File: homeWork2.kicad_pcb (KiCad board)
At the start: 2 copper layers, 130 x 100 mm, 49 parts, among them J1 Barrel_Jack_Switch_SMT, J2 0.100_2Pin, J3 0.100_2Pin, U1 LM7805_TO220

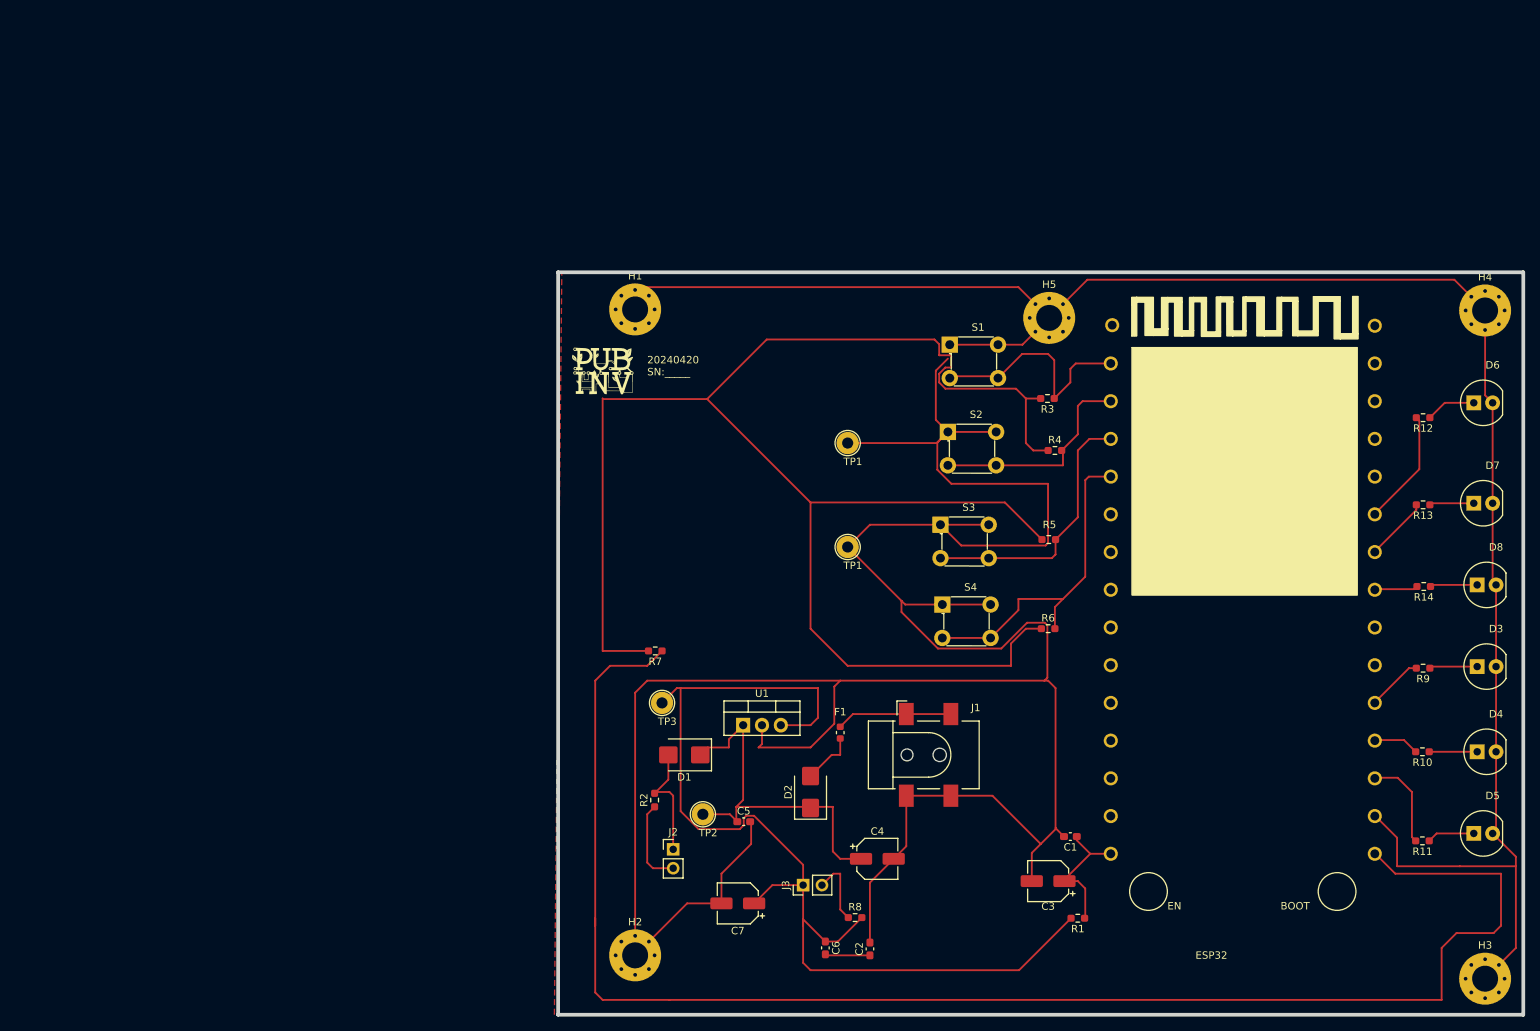
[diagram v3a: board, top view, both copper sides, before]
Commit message: I removed the ground traces and applied copper fill on both the front and back copper layers to establish the ground connections. Additionally, I updated the footprint of the ESP32, positioning the antenna within an area free from copper ground connections, and added four holes along its edges.
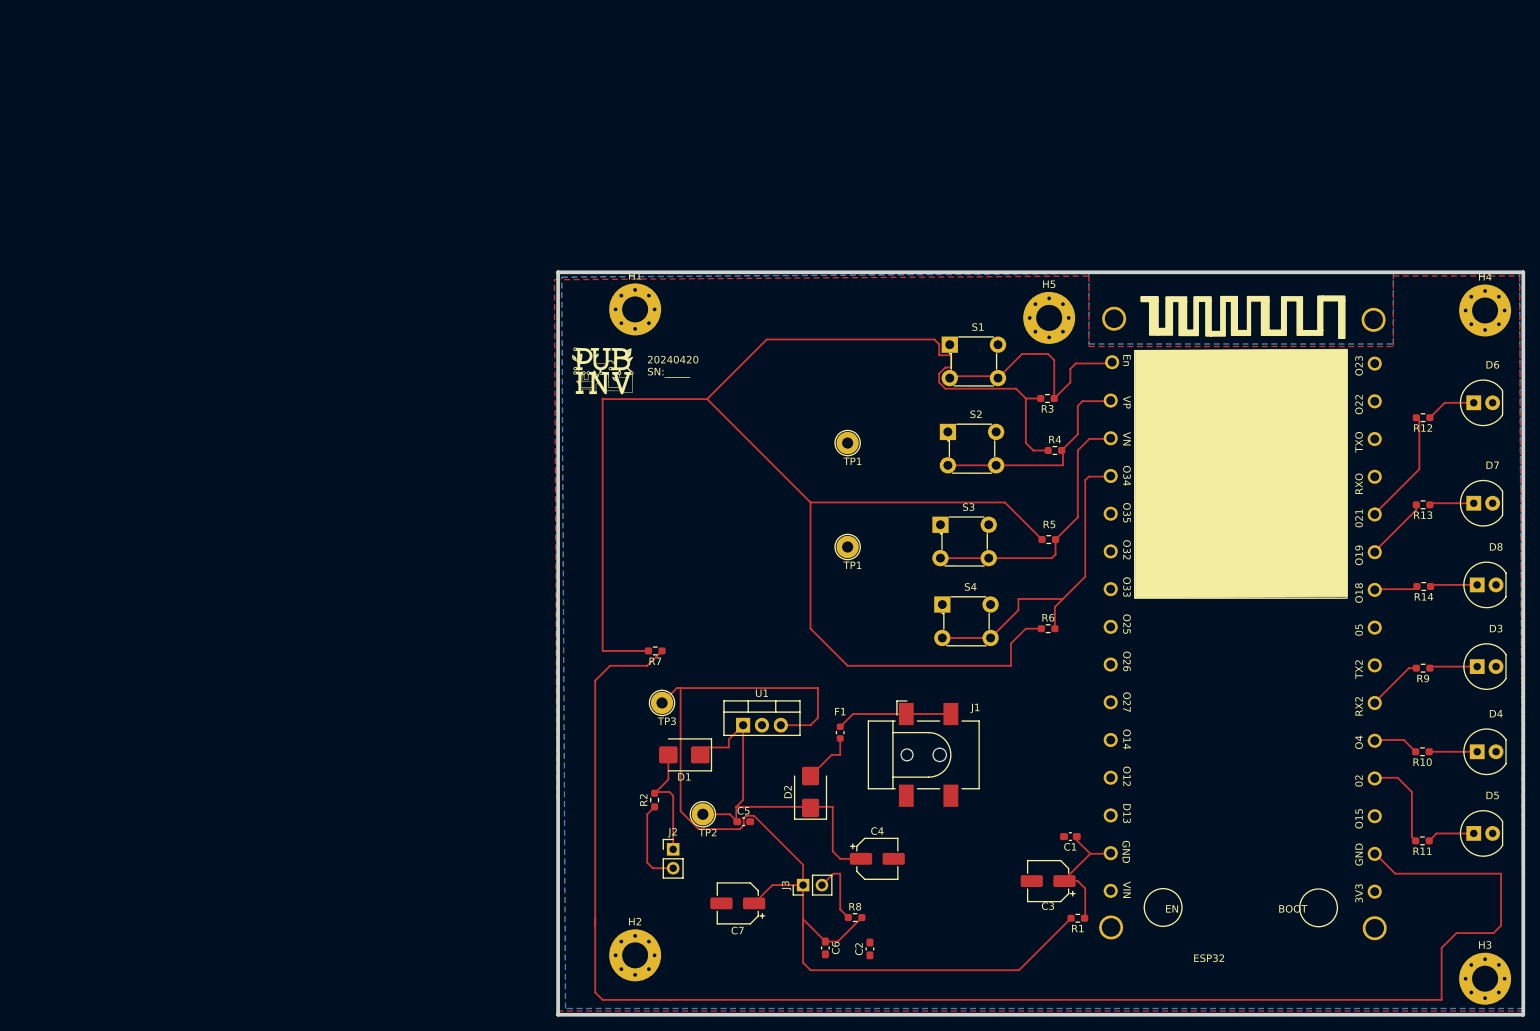
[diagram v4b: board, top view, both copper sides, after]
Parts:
- moved ESP32 0.53 mm to (211.9, 47.5)
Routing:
- net GND: track 625.6 -> 0.19 mm
- added copper zone on B.Cu, net GND

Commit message: I updated the ESP32 footprint and symbol, renamed the pins of the ESP32 in a clockwise direction. I rerouted the copper, and ran a DRC test with zero errors and refined the edge cut of the board to make it smaller and neater.
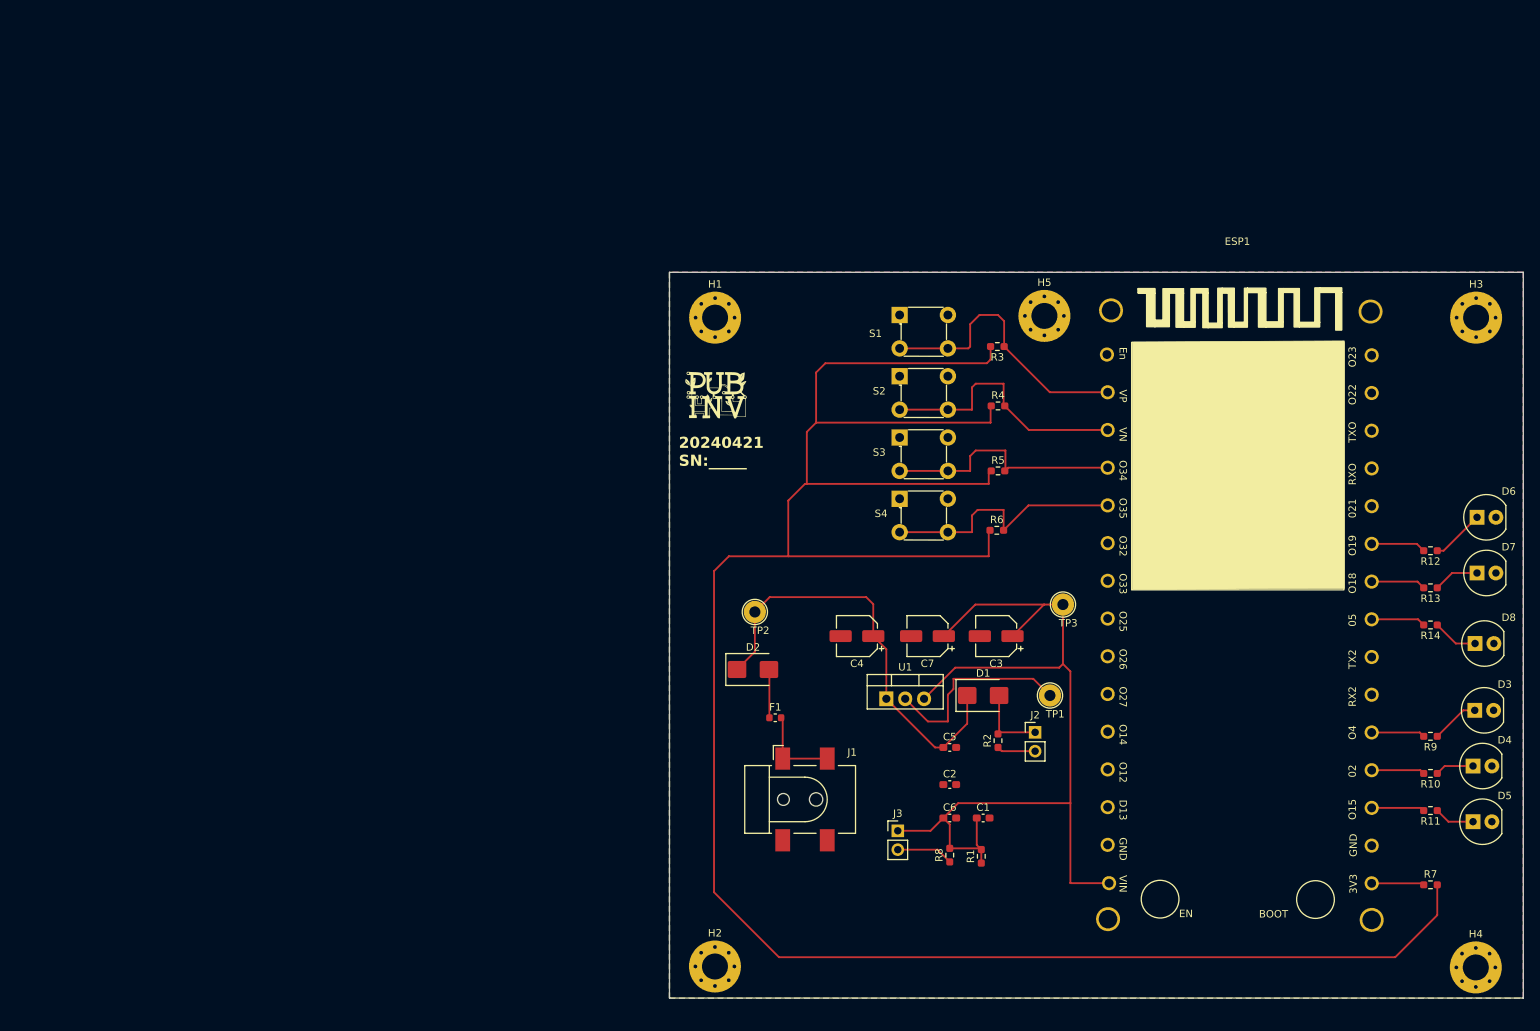
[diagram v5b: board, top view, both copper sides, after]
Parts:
- removed ESP32: Wroom ESP32, esp32 15 pin Library:esp32
- removed the TP1 at (159.0, 73.0)
- removed the TP1 at (159.0, 87.0)
- added ESP1: ~, esp32 15 pin Library:esp32, F.Cu at (211.5, 46.3)
- added TP1: TestPoint, TestPoint:TestPoint_Loop_D2.54mm_Drill1.5mm_Beaded, F.Cu at (186.2, 107.0)
- C1, C5, C6: value 100nF -> C
- C2: value 39pF -> C
- C3, C4, C7: value 47uF 16V -> C_Polarized
- D1, D2: value Schottky 2A -> D_Schottky
- R1, R7: value 1R0 -> R
- R10, R11, R12, R13, R14, R9: value 330R -> R
- R2, R8: value DNI -> R
- R3, R4, R5, R6: value 10K -> R
- TP2: value Vin -> TestPoint
- TP3: value +5V -> TestPoint
- moved R7 109.1 mm to (237.5, 132.5), turned to 0 degrees
- moved H3 89.0 mm to (243.6, 56.1)
- moved H4 88.5 mm to (243.6, 143.6)
- moved TP3 55.6 mm to (188.0, 94.8)
- moved J2 51.2 mm to (184.2, 112.0)
- moved R2 46.9 mm to (179.2, 113.1)
- moved C7 44.1 mm to (169.8, 99.0)
- moved D1 41.0 mm to (177.2, 107.0), turned to 0 degrees
- moved C3 33.7 mm to (179.0, 99.0)
- moved C4 30.1 mm to (160.2, 99.0), turned to 180 degrees
- moved C5 29.5 mm to (172.8, 114.0)
- moved TP2 28.1 mm to (146.5, 95.8)
- moved C2 24.6 mm to (172.8, 119.0), turned to 0 degrees
- moved C6 24.2 mm to (172.8, 123.5), turned to 0 degrees
- moved U1 19.6 mm to (164.2, 107.4)
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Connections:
- C1 pad 1: Net-(ESP1-VIN) -> +5V
- C3 pad 1: Net-(ESP1-VIN) -> +5V
- R1 pad 1: Net-(ESP1-VIN) -> +5V
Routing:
- net Net-(ESP1-3V3): track 209.6 -> 7.09 mm
- net +3.3V: track 227.9 -> 296.7 mm
- net GND: track 0.19 -> 27.0 mm
- net Net-(ESP1-VIN): track 18.2 -> 0.00 mm
- net +5V: track 140.9 -> 127.5 mm
- net Net-(ESP1-O35): track 44.6 -> 34.7 mm
- net Vin: track 49.9 -> 58.1 mm
- net Net-(ESP1-O19): track 15.6 -> 7.39 mm
- net ControllerVcc: track 11.7 -> 5.21 mm
- net Net-(ESP1-VP): track 31.6 -> 38.0 mm
- net Net-(ESP1-VN): track 29.2 -> 35.5 mm
- net Net-(D1-A): track 15.9 -> 10.3 mm
- net Net-(ESP1-O15): track 12.6 -> 7.16 mm
- net Net-(F1-Pad2): track 15.6 -> 11.6 mm
- net Net-(ESP1-O34): track 36.0 -> 33.4 mm
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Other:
- board size 130 x 100 mm -> 115 x 97.8 mm
- board text added: "20240421 SN:_____"
- board text removed: "20240420 SN:_____"

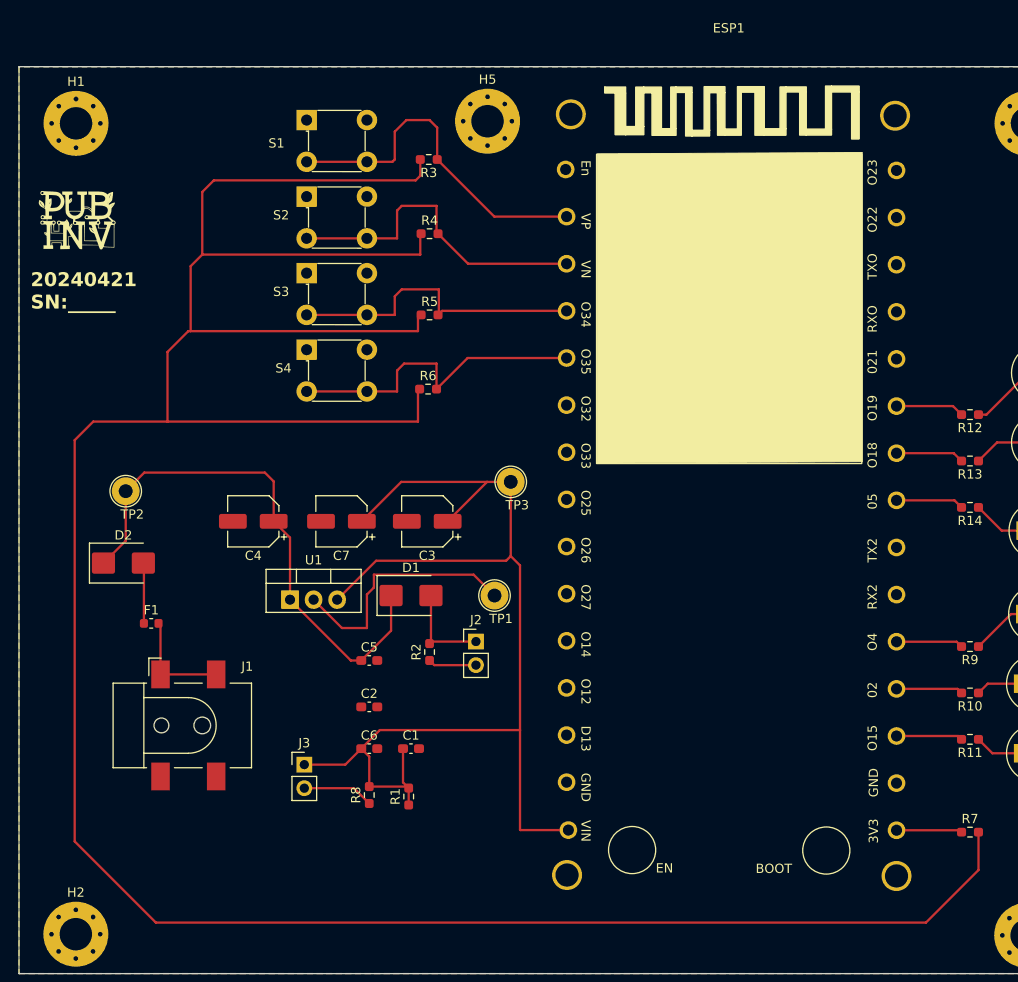
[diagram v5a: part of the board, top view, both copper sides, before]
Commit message: the Barrel Jack is moved to the edge of the board. the copper ainfront of the antenna of the ESP32 is removed, the copper connecting the components to ESP32 is rerouted and routed on the back copper layer through via to the front copper layer of the board, and the ESP32 footprint is updated to place the pin names of the ESP32 on the back silkscreen layer.
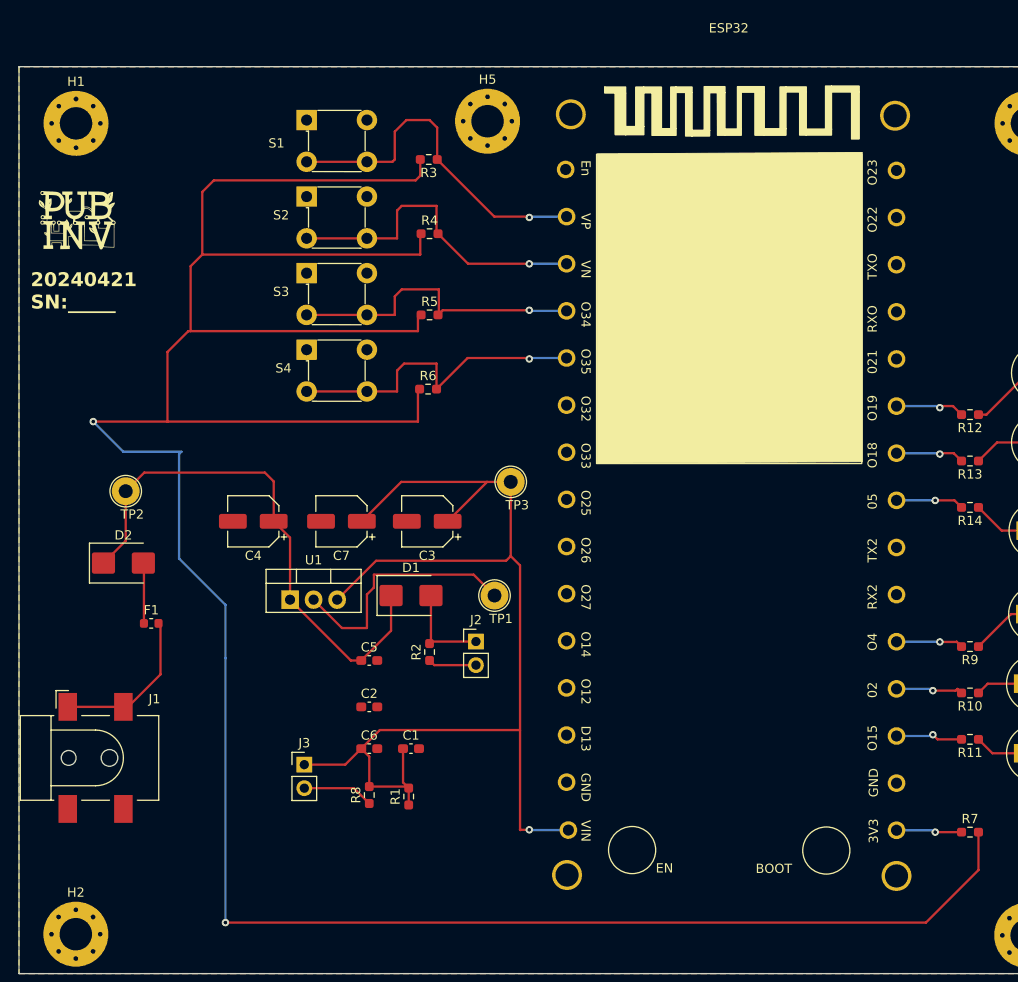
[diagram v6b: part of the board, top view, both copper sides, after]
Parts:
- moved J1 10.6 mm to (143.2, 124.5)
- renumbered ESP1 to ESP32
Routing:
- net Net-(F1-Pad2): track 11.6 -> 17.0 mm
- net +3.3V: track 296.7 -> 294.3 mm, vias 0 -> 2
- net +5V: track 127.5 -> 127.8 mm, vias 0 -> 1
- net Net-(ESP1-O2): track 7.19 -> 7.35 mm, vias 0 -> 1
- net Net-(ESP1-O19): track 7.39 -> 7.53 mm, vias 0 -> 1
- net Net-(ESP1-O15): track 7.16 -> 7.27 mm, vias 0 -> 1
- net Net-(ESP1-O35): track 34.7 -> 34.8 mm, vias 0 -> 1
- net Net-(ESP1-VP): vias 0 -> 1
- net Net-(ESP1-O18): track 7.36 -> 7.43 mm, vias 0 -> 1
- net Net-(ESP1-O34): vias 0 -> 1
- net Net-(ESP1-O4): track 7.22 -> 7.24 mm, vias 0 -> 1
- net Net-(ESP1-VN): vias 0 -> 1
- net Net-(ESP1-O5): track 7.32 -> 7.33 mm, vias 0 -> 1
- net Net-(ESP1-3V3): vias 0 -> 1
